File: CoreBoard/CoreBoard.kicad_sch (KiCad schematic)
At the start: 57 parts, among them J1 RJ45_LED_Shielded, SW1 SW_Push, SW2 SW_Push, SW3 SW_Push, SW4 SW_Push, SW5 SW_Push, SW6 SW_Push, SW7 SW_Push, SW8 SW_Push, SW9 SW_Push, U1 OKI, U2 Teensy4.1_DEV-16771, U3 SHHD003A0A, U4 GY-521

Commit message: Small changes
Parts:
- added SW10: SW_DIP_x07, symbol Switch:SW_DIP_x07
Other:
- note added: "CAN Connection"
- note added: "Dip Switch"
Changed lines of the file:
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@@
 		)
 	)
+	(polyline
+		(pts
+			(xy 248.92 139.7) (xy 285.75 139.7)
+		)
+		(stroke
+			(width 0)
+			(type default)
+		)
+	)
 	(wire
 		(pts
@@
 		)
 	)
+	(polyline
+		(pts
+			(xy 285.75 12.7) (xy 285.75 76.2)
+		)
+		(stroke
+			(width 0)
+			(type default)
+		)
+	)
 	(wire
 		(pts
@@
 		)
 	)
+	(polyline
+		(pts
+			(xy 285.75 139.7) (xy 285.75 76.2)
+		)
+		(stroke
+			(width 0)
+			(type default)
+		)
+	)
 	(wire
 		(pts
@@
 		)
 	)
+	(polyline
+		(pts
+			(xy 185.42 76.2) (xy 285.75 76.2)
+		)
+		(stroke
+			(width 0)
+			(type default)
+		)
+	)
 	(wire
 		(pts
@@
 		)
 	)
+	(text "CAN Connection"
+		(exclude_from_sim no)
+		(at 327.406 82.042 0)
+		(effects
+			(font
+				(size 5.08 5.08)
+			)
+		)
+	)
+	(text "Dip Switch"
+		(exclude_from_sim no)
+		(at 233.934 86.614 0)
+		(effects
+			(font
+				(size 5.08 5.08)
+			)
+		)
+	)
 	(label "Encoders"
 		(at 313.69 26.67 0)
@@
 					(unit 1)
 				)
+			)
+		)
+	)
+	(symbol
+		(lib_id "Switch:SW_DIP_x07")
+		(at 234.95 111.76 0)
+		(unit 1)
+		(exclude_from_sim no)
+		(in_bom yes)
+		(on_board yes)
+		(dnp no)
+		(fields_autoplaced yes)
+		(property "Reference" "SW10"
+			(at 234.95 96.52 0)
+			(effects
+				(font
+					(size 1.27 1.27)
+				)
+			)
+		)
+		(property "Value" "SW_DIP_x07"
+			(at 234.95 99.06 0)
+			(effects
+				(font
+					(size 1.27 1.27)
+				)
+			)
+		)
+		(property "Footprint" ""
+			(at 234.95 114.3 0)
+			(effects
+				(font
+					(size 1.27 1.27)
+				)
+				(hide yes)
+			)
+		)
+		(property "Datasheet" "~"
+			(at 234.95 114.3 0)
+			(effects
+				(font
+					(size 1.27 1.27)
+				)
+				(hide yes)
+			)
+		)
+		(property "Description" "7x DIP Switch, Single Pole Single Throw (SPST) switch, small symbol"
+			(at 234.95 111.76 0)
+			(effects
+				(font
+					(size 1.27 1.27)
+				)
+				(hide yes)
+			)
+		)
+		(pin "11"
+		)
+		(pin "6"
+		)
+		(pin "12"
+		)
+		(pin "2"
+		)
+		(pin "9"
+		)
+		(pin "7"
+		)
+		(pin "14"
+		)
+		(pin "1"
+		)
+		(pin "13"
+		)
+		(pin "3"
+		)
+		(pin "5"
+		)
+		(pin "4"
+		)
+		(pin "10"
+		)
+		(pin "8"
+		)
+		(instances
+			(project ""
+				(path "/235fe3cd-a03a-419e-9e89-7ef0b61e68dc"
+					(reference "SW10")
+					(unit 1)
+				)

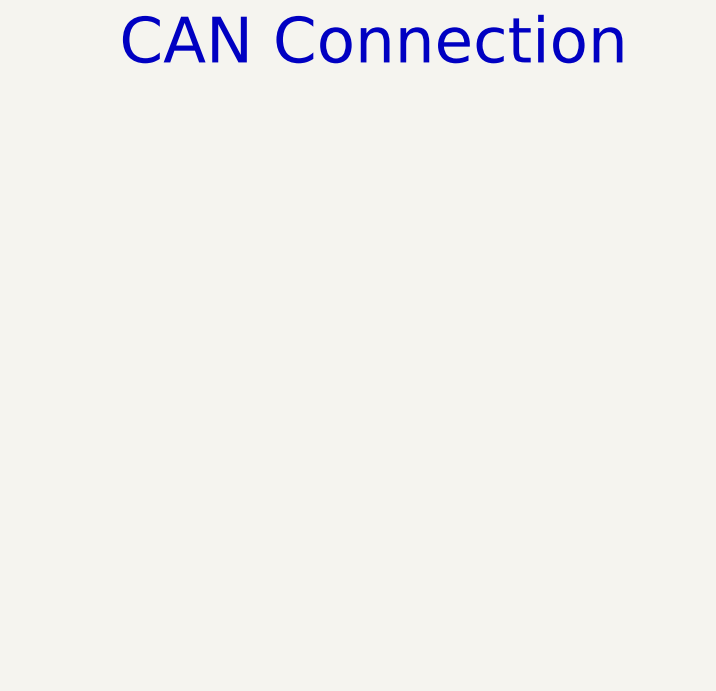
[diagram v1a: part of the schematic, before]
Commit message: Added CAN Transmitter
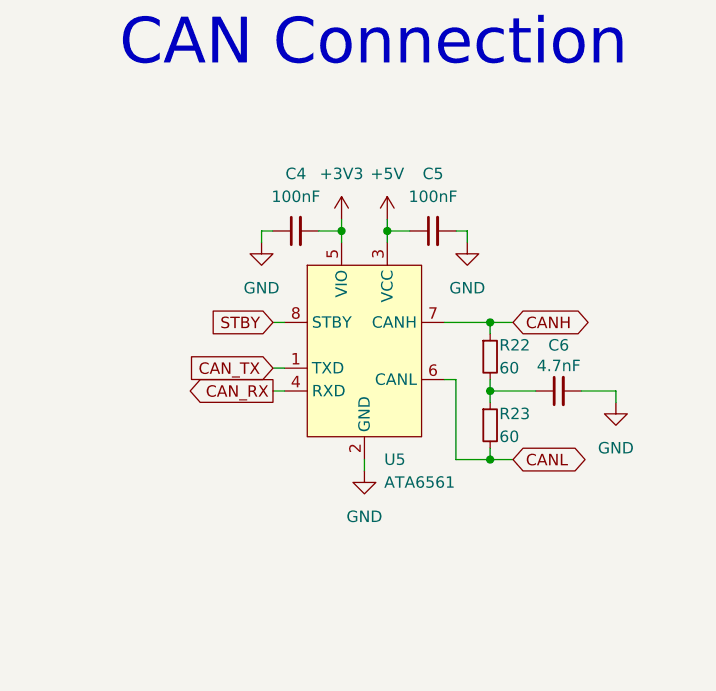
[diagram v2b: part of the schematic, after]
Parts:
- added C4, C5: 100nF, symbol Device:C_Small
- added C6: 4.7nF, symbol Device:C_Small
- added R22, R23: 60, symbol Device:R_Small
- added U5: ATA6561, Package_SO:SOIC-8_3.9x4.9mm_P1.27mm, symbol MRDT_Devices:ATA6561
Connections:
- net +5V: now also C5.1, U5.3 (VCC)
- net GND: now also C4.1, C5.2, C6.2, U5.2 (GND)
- new net: C6.1, R22.2, R23.1
- new net +3V3: C4.2, U5.5 (VIO)
- new net CANH: R22.1, U5.7 (CANH)
- new net CANL: R23.2, U5.6 (CANL)
- new net CAN_RX: U5.4 (RXD)
- new net CAN_TX: U5.1 (TXD)
- new net STBY: U5.8 (STBY)

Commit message: Added Encoders, 8 switch dipswitch, and Teensy inputs and outputs
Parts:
- removed SW10: SW_DIP_x07, symbol Switch:SW_DIP_x07
- added SW10: SW_DIP_x08, symbol Switch:SW_DIP_x08
- added U6, U7: 74HC148, Package_SO:SOIC-16_4.55x10.3mm_P1.27mm, symbol 74xx:74LS148
- added U8: 74HC00, symbol 74xx:74HC00
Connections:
- net +3.3V: now also U6.16 (VCC), U7.10 (IO), U7.16 (VCC), U8.14 (VCC)
- net +5V: now also U2.VIN
- net AccSCL: now also U2.19 (A5)
- net AccSDA: now also U2.18 (A4)
- net B1: now also U7.11 (I1)
- net B2: now also U7.12 (I2)
- net B3: now also U7.13 (I3)
- net B4: now also U7.1 (I4)
- net B5: now also U7.2 (I5)
- net B6: now also U7.3 (I6)
- net B7: now also U7.4 (I7)
- net B8: now also U6.10 (IO)
- net B9: now also U6.11 (I1)
- net BL_RX: now also U2.34 (RX8)
- net BL_TX: now also U2.35 (TX8)
- net BR_RX: now also U2.15 (A1)
- net BR_TX: now also U2.14 (A0)
- net FL_RX: now also U2.28 (RX7)
- net FL_TX: now also U2.29 (TX7)
- net FR_RX: now also U2.21 (A7)
- net FR_TX: now also U2.20 (A6)
- net GND: now also U6.5 (EI), U6.8 (GND), U7.8 (GND), U8.7 (GND)
- net ML_RX: now also U2.25 (A11)
- net ML_TX: now also U2.24 (A10)
- net MR_RX: now also U2.16 (A2)
- net MR_TX: now also U2.17 (A3)
- net ServoPWM1: now also U2.0 (RX1)
- net ServoPWM2: now also U2.1 (TX1)
- net ServoPWM3: now also U2.2 (OUT2)
- net ServoPWM4: now also U2.3 (LRCLK2)
- net ServoPWM5: now also U2.4 (BCLK2)
- net ServoPWM6: now also U2.5 (IN2)
- net ServoPWM7: now also U2.6 (OUT1D)
- net ServoPWM8: now also U2.7 (RX2)
- net ServoPWM9: now also U2.8 (TX2)
- net Out1: now reaches U2.22 (A8)
- net Out1: now also U8.6
- net Out0: now reaches U2.23 (A9)
- net Out0: now also U8.3
- net Out3: now reaches U2.33 (MCLK2)
- net Out3: now also U6.15 (EO), U7.5 (EI)
- net Out2: now reaches U2.41 (A17)
- net Out2: now also U8.8
- new net: U6.7 (S1), U8.4
- new net: U7.7 (S1), U8.5
- new net: U6.9 (S0), U8.1
- new net: U7.9 (S0), U8.2
- new net: U6.6 (S2), U8.9
- new net: U7.6 (S2), U8.10
- new net B10: U6.12 (I2)
- no-connect marks 4 -> 10
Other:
- moved on the sheet: C3, C4, C5, C6, D10, D11, D12, D4, D5, D6, D7, D8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

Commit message: Added CAN connections to Teensy
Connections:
- net CAN_RX: now also U2.30 (CRX3)
- net CAN_TX: now also U2.31 (CTX3)
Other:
- moved on the sheet: SW10
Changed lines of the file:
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@@
 	(wire
 		(pts
+			(xy 45.72 226.06) (xy 46.99 226.06)
+		)
+		(stroke
+			(width 0)
+			(type default)
+		)
+	)
+	(wire
+		(pts
 			(xy 350.52 119.38) (xy 365.76 119.38)
 		)
@@
 	(wire
 		(pts
+			(xy 45.72 223.52) (xy 46.99 223.52)
+		)
+		(stroke
+			(width 0)
+			(type default)
+		)
+	)
+	(wire
+		(pts
 			(xy 49.53 107.95) (xy 54.61 107.95)
 		)
@@
 	(text "Dip Switch"
 		(exclude_from_sim no)
-		(at 364.744 184.404 0)
+		(at 355.346 148.336 0)
 		(effects
 			(font
@@
 		)
 	)
+	(global_label "CAN_RX"
+		(shape input)
+		(at 45.72 223.52 180)
+		(fields_autoplaced yes)
+		(effects
+			(font
+				(size 1.27 1.27)
+			)
+			(justify right)
+		)
+		(property "Intersheetrefs" "${INTERSHEET_REFS}"
+			(at 35.5986 223.52 0)
+			(effects
+				(font
+					(size 1.27 1.27)
+				)
+				(justify right)
+				(hide yes)
+			)
+		)
+	)
 	(global_label "B9"
 		(shape input)
@@
 		)
 	)
+	(global_label "CAN_TX"
+		(shape output)
+		(at 45.72 226.06 180)
+		(fields_autoplaced yes)
+		(effects
+			(font
+				(size 1.27 1.27)
+			)
+			(justify right)
+		)
+		(property "Intersheetrefs" "${INTERSHEET_REFS}"
+			(at 35.901 226.06 0)
+			(effects
+				(font
+					(size 1.27 1.27)
+				)
+				(justify right)
+				(hide yes)
+			)
+		)
+	)
 	(global_label "ServoPWM3"
 		(shape output)
@@
 	(symbol
 		(lib_id "Switch:SW_DIP_x08")
-		(at 364.49 210.82 0)
+		(at 350.52 200.66 0)
 		(unit 1)
 		(exclude_from_sim no)
@@
 		(fields_autoplaced yes)
 		(property "Reference" "SW10"
-			(at 364.49 193.04 0)
+			(at 350.52 182.88 0)
 			(effects
 				(font
@@
 		)
 		(property "Value" "SW_DIP_x08"
-			(at 364.49 195.58 0)
+			(at 350.52 185.42 0)
 			(effects
 				(font
@@
 		)
 		(property "Footprint" ""
-			(at 364.49 210.82 0)
+			(at 350.52 200.66 0)
 			(effects
 				(font
@@
 		)
 		(property "Datasheet" "~"
-			(at 364.49 210.82 0)
+			(at 350.52 200.66 0)
 			(effects
 				(font
@@
 		)
 		(property "Description" "8x DIP Switch, Single Pole Single Throw (SPST) switch, small symbol"
-			(at 364.49 210.82 0)
+			(at 350.52 200.66 0)
 			(effects
 				(font

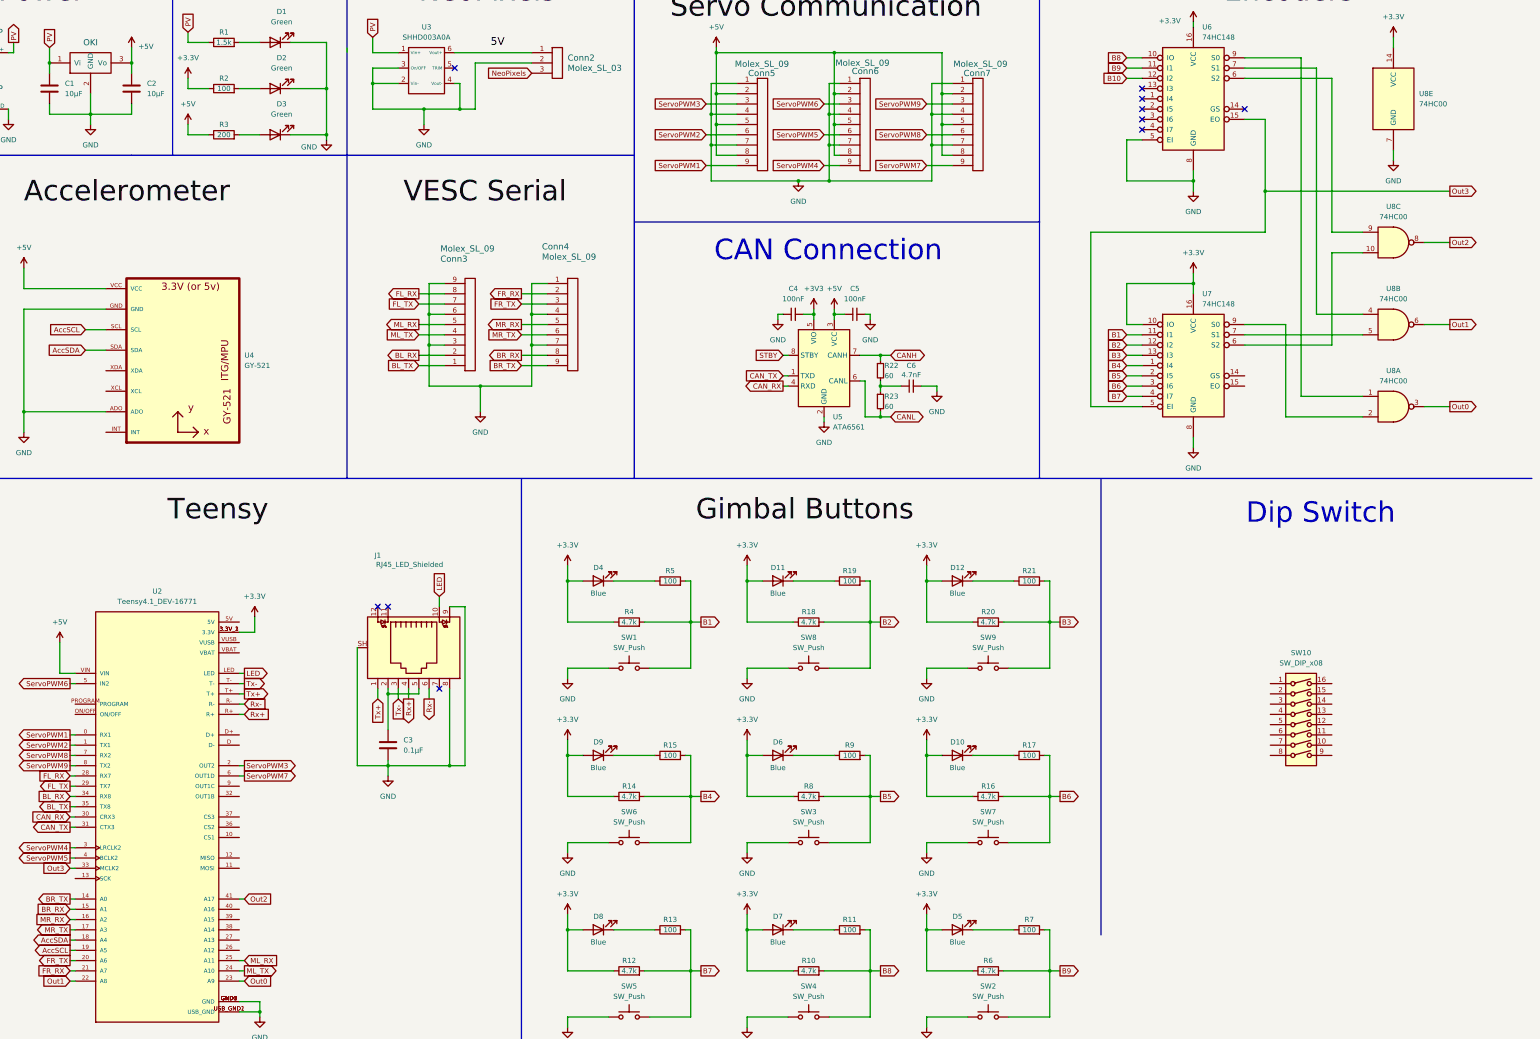
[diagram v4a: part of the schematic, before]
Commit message: Added connections from the dip switch and button to the Teensy, and from the Teensy to the encoder. Schematics should be finished for now
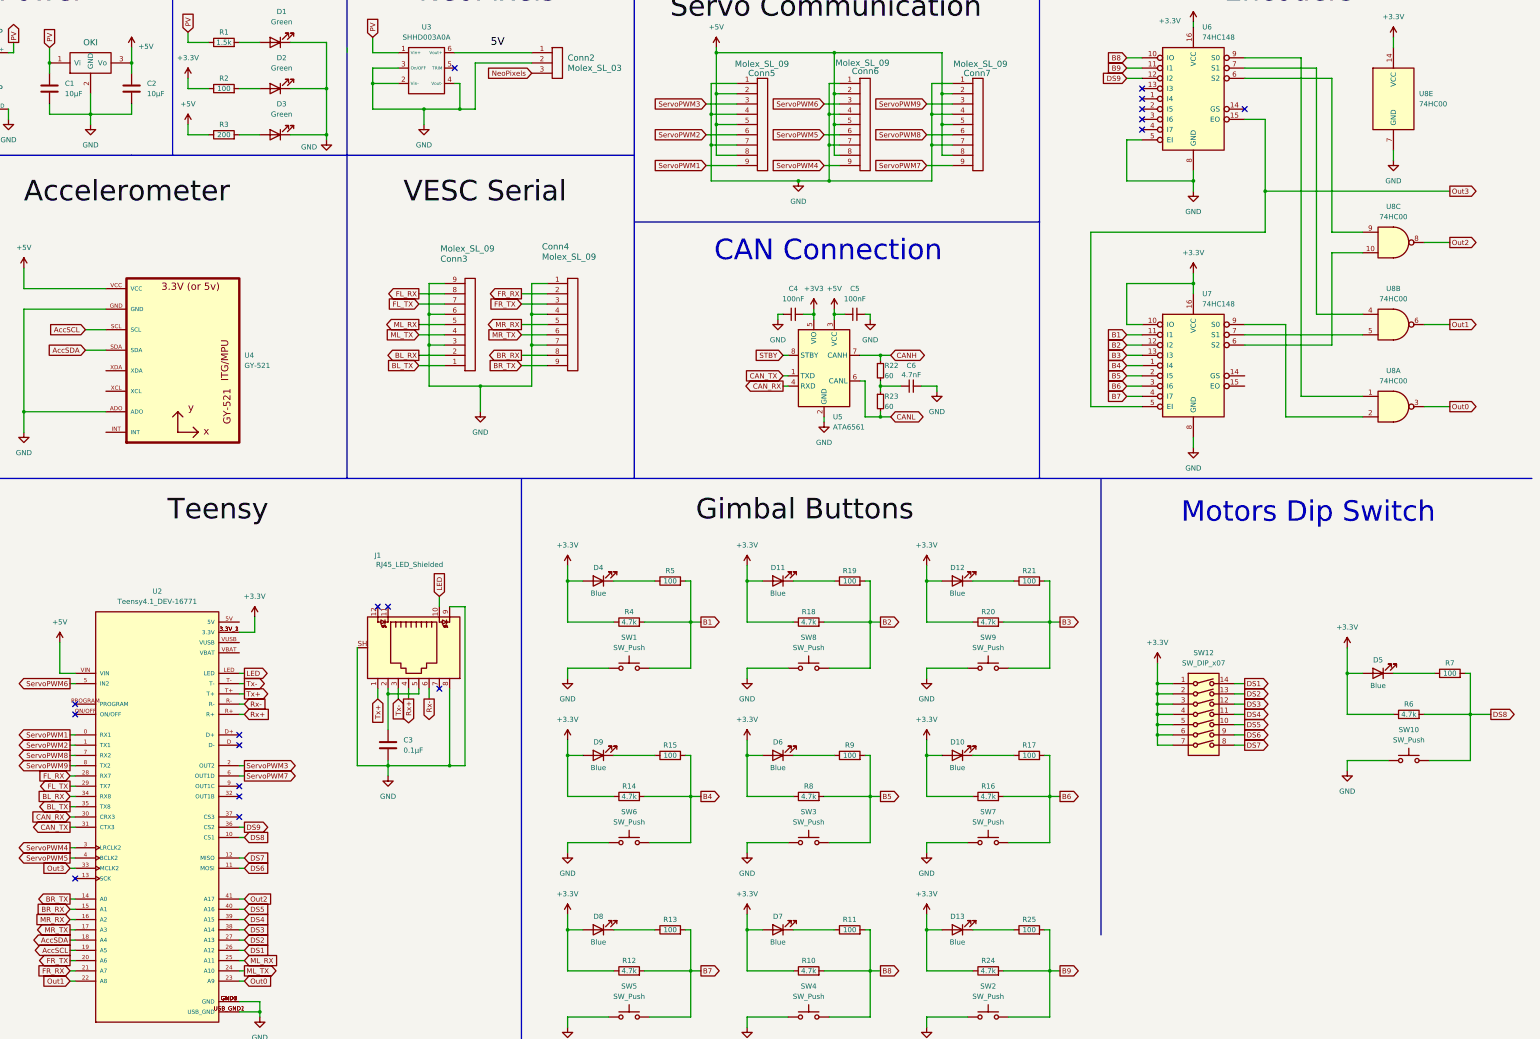
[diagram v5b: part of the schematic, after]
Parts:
- removed SW10: SW_DIP_x08, symbol Switch:SW_DIP_x08
- added D13: Blue, symbol Device:LED
- added R24: 4.7k, symbol Device:R
- added R25: 100, symbol Device:R
- added SW10: SW_Push, symbol Switch:SW_Push
- added SW12: SW_DIP_x07, symbol Switch:SW_DIP_x07
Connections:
- net B10 is gone; now on net DS9: U6.12 (I2)
- net +3.3V: now also D13.2 (A), R24.1, SW12.1, SW12.2, SW12.3, SW12.4, SW12.5, SW12.6, SW12.7
- net B9: now also R24.2, R25.2; no longer R6.2, R7.2
- net GND: now also SW10.1
- net DS8: now reaches U2.10 (CS1)
- net DS8: now also R6.2, R7.2, SW10.2
- net DS6: now reaches U2.11 (MOSI)
- net DS6: now also SW12.9
- net DS7: now reaches U2.12 (MISO)
- net DS7: now also SW12.8
- net DS1: now reaches U2.26 (A12)
- net DS1: now also SW12.14
- net DS2: now reaches U2.27 (A13)
- net DS2: now also SW12.13
- net DS9: now reaches U2.36 (CS2)
- net DS3: now reaches U2.38 (A14)
- net DS3: now also SW12.12
- net DS4: now reaches U2.39 (A15)
- net DS4: now also SW12.11
- net DS5: now reaches U2.40 (A16)
- net DS5: now also SW12.10
- new net: D13.1 (K), R25.1
- no-connect marks 10 -> 18
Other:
- note added: "Motors Dip Switch"
- note removed: "Dip Switch"

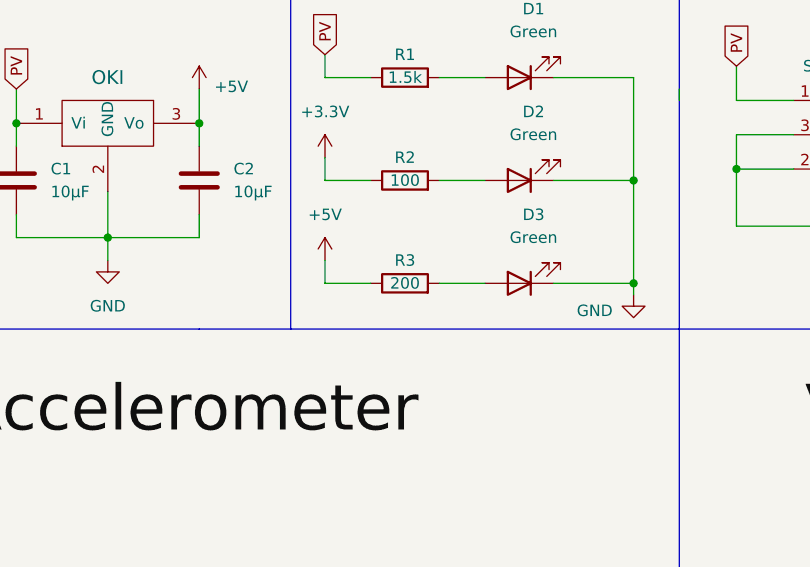
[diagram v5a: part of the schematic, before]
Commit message: Swapped 200 ohm resistor for 220 ohm resistor
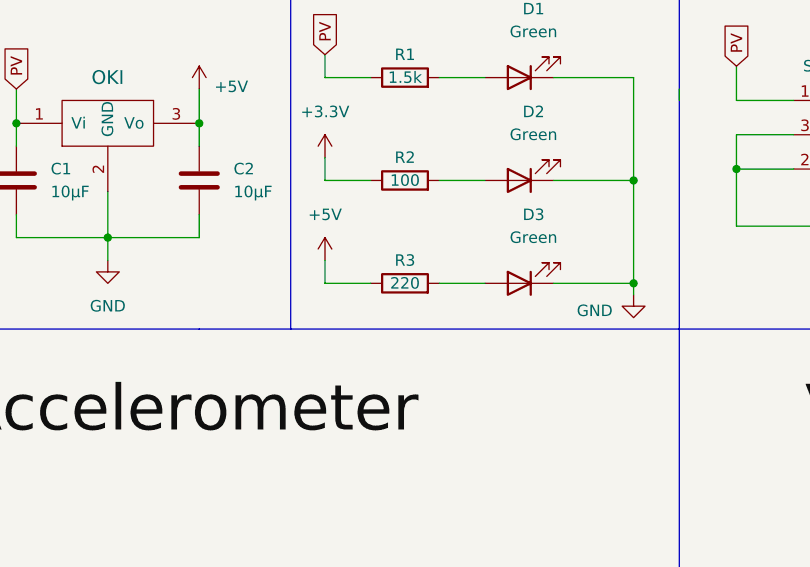
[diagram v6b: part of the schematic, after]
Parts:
- R3: value 200 -> 220
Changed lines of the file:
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@@
 			)
 		)
-		(property "Value" "200"
+		(property "Value" "220"
 			(at 83.82 54.61 90)
 			(effects

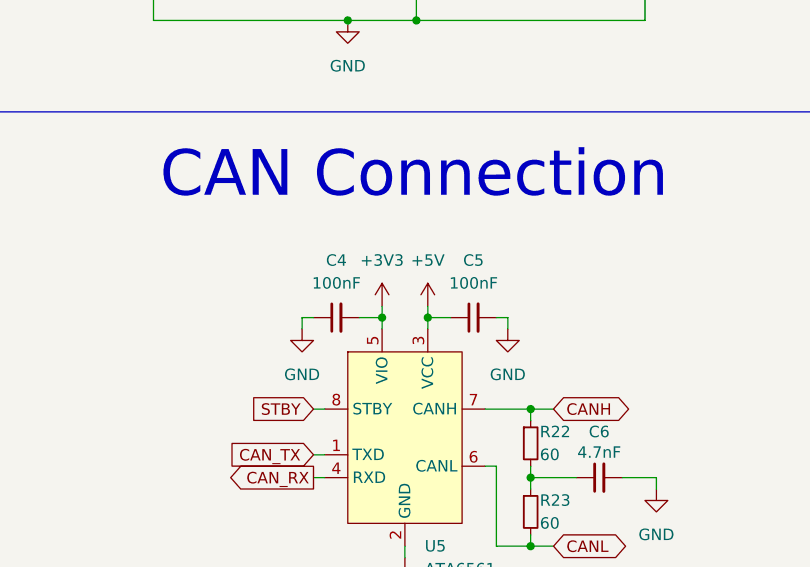
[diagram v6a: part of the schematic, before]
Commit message: Changed 100nF capacitors to 0.1µF capacitors
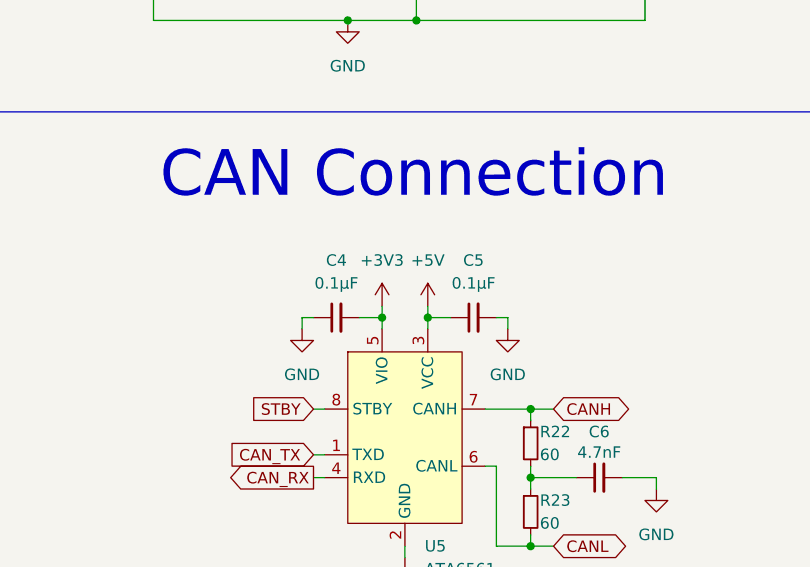
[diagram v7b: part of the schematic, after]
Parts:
- C4, C5: value 100nF -> 0.1µF
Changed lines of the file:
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@@
 			)
 		)
-		(property "Value" "100nF"
+		(property "Value" "0.1µF"
 			(at 224.7963 95.25 90)
 			(effects
@@
 			)
 		)
-		(property "Value" "100nF"
+		(property "Value" "0.1µF"
 			(at 240.0363 95.25 90)
 			(effects
